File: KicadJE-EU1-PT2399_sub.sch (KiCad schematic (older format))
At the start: 57 parts, among them J201 In, J202 Out, P201 HEADER_2x5_Doepfer, Q201 BC337, Q202 PZT2222A, Q203 PZT2222A, U201 TL072, U202 PT2399

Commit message: Footprints
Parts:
- RV201: footprint Potentiometer_THT:Potentiometer_Alps_RK09K_Single_Vertical -> Potentiometer_THT:Potentiometer_China_RK09_Single_Vertical_AJ
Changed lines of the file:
@@
 	2550 1250 2550 1350
 $Comp
-L Eurorack:HEADER_2x5_Doepfer P201
+L Eurorack:HEADER_2x5_Doepfer P?
 U 1 1 5D631512
 P 2800 1350
-AR Path="/5D631512" Ref="P201"  Part="1"
+AR Path="/5D631512" Ref="P?"  Part="1"
 AR Path="/5D60ED9A/5D631512" Ref="P201"  Part="1"
 F 0 "P201" H 2800 852 40  0000 C CNN
@@
 	4050 1800 3725 1800
 $Comp
-L power:+5VA #PWR0201
+L power:+5VA #PWR0121
 U 1 1 5D64AB64
 P 4575 1150
-F 0 "#PWR0201" H 4575 1000 50  0001 C CNN
+F 0 "#PWR0121" H 4575 1000 50  0001 C CNN
 F 1 "+5VA" H 4590 1323 50  0000 C CNN
 F 2 "" H 4575 1150 50  0001 C CNN
@@
 $EndComp
 $Comp
-L power:+5VA #PWR0209
+L power:+5VA #PWR0122
 U 1 1 5D64D016
 P 3725 3550
-F 0 "#PWR0209" H 3725 3400 50  0001 C CNN
+F 0 "#PWR0122" H 3725 3400 50  0001 C CNN
 F 1 "+5VA" H 3740 3723 50  0000 C CNN
 F 2 "" H 3725 3550 50  0001 C CNN
@@
 Connection ~ 4425 1800
 $Comp
-L power:GNDA #PWR0206
+L power:GNDA #PWR0123
 U 1 1 5D64E4DB
 P 4425 2100
-F 0 "#PWR0206" H 4425 1850 50  0001 C CNN
+F 0 "#PWR0123" H 4425 1850 50  0001 C CNN
 F 1 "GNDA" H 4430 1927 50  0000 C CNN
 F 2 "" H 4425 2100 50  0001 C CNN
@@
 Connection ~ 4425 2100
 $Comp
-L power:GNDA #PWR0210
+L power:GNDA #PWR0124
 U 1 1 5D64E67F
 P 3425 3850
-F 0 "#PWR0210" H 3425 3600 50  0001 C CNN
+F 0 "#PWR0124" H 3425 3600 50  0001 C CNN
 F 1 "GNDA" H 3430 3677 50  0000 C CNN
 F 2 "" H 3425 3850 50  0001 C CNN
@@
 	3725 4450 3550 4450
 $Comp
-L power:GNDA #PWR0218
+L power:GNDA #PWR0125
 U 1 1 5D653327
 P 3700 4875
-F 0 "#PWR0218" H 3700 4625 50  0001 C CNN
+F 0 "#PWR0125" H 3700 4625 50  0001 C CNN
 F 1 "GNDA" H 3705 4702 50  0000 C CNN
 F 2 "" H 3700 4875 50  0001 C CNN
@@
 $EndComp
 $Comp
-L power:GNDA #PWR0217
+L power:GNDA #PWR0126
 U 1 1 5D653368
 P 3550 4750
-F 0 "#PWR0217" H 3550 4500 50  0001 C CNN
+F 0 "#PWR0126" H 3550 4500 50  0001 C CNN
 F 1 "GNDA" H 3555 4577 50  0000 C CNN
 F 2 "" H 3550 4750 50  0001 C CNN
@@
 Connection ~ 5675 4250
 $Comp
-L power:GNDA #PWR0215
+L power:GNDA #PWR0127
 U 1 1 5D6610CC
 P 5675 4450
-F 0 "#PWR0215" H 5675 4200 50  0001 C CNN
+F 0 "#PWR0127" H 5675 4200 50  0001 C CNN
 F 1 "GNDA" H 5680 4277 50  0000 C CNN
 F 2 "" H 5675 4450 50  0001 C CNN
@@
 $EndComp
 $Comp
-L power:GNDA #PWR0212
+L power:GNDA #PWR0128
 U 1 1 5D667A82
 P 5150 3975
-F 0 "#PWR0212" H 5150 3725 50  0001 C CNN
+F 0 "#PWR0128" H 5150 3725 50  0001 C CNN
 F 1 "GNDA" H 5155 3802 50  0000 C CNN
 F 2 "" H 5150 3975 50  0001 C CNN
@@
 F 0 "RV201" H 6075 3775 50  0000 R CNN
 F 1 "50k" H 6075 3850 50  0000 R CNN
-F 2 "Potentiometer_THT:Potentiometer_Alps_RK09K_Single_Vertical" H 5850 3925 50  0001 C CNN
+F 2 "Potentiometer_THT:Potentiometer_China_RK09_Single_Vertical_AJ" H 5850 3925 50  0001 C CNN
 F 3 "~" H 5850 3925 50  0001 C CNN
 	1    5850 3925
@@
 	5675 3775 5850 3775
 $Comp
-L power:GNDA #PWR0213
+L power:GNDA #PWR0129
 U 1 1 5D66F427
 P 5850 4075
-F 0 "#PWR0213" H 5850 3825 50  0001 C CNN
+F 0 "#PWR0129" H 5850 3825 50  0001 C CNN
 F 1 "GNDA" H 5950 3950 50  0000 C CNN
 F 2 "" H 5850 4075 50  0001 C CNN
@@
 $EndComp
 $Comp
-L power:GNDA #PWR0207
+L power:GNDA #PWR0130
 U 1 1 5D6945A7
 P 5025 3100
-F 0 "#PWR0207" H 5025 2850 50  0001 C CNN
+F 0 "#PWR0130" H 5025 2850 50  0001 C CNN
 F 1 "GNDA" H 5030 2927 50  0000 C CNN
 F 2 "" H 5025 3100 50  0001 C CNN
@@
 $EndComp
 $Comp
-L power:GNDA #PWR0208
+L power:GNDA #PWR0131
 U 1 1 5D694740
 P 6250 3375
-F 0 "#PWR0208" H 6250 3125 50  0001 C CNN
+F 0 "#PWR0131" H 6250 3125 50  0001 C CNN
 F 1 "GNDA" H 6255 3202 50  0000 C CNN
 F 2 "" H 6250 3375 50  0001 C CNN
@@
 	2650 4300 2650 4375
 $Comp
-L power:+5VA #PWR0214
+L power:+5VA #PWR0132
 U 1 1 5D6D7FCA
 P 2525 4375
-F 0 "#PWR0214" H 2525 4225 50  0001 C CNN
+F 0 "#PWR0132" H 2525 4225 50  0001 C CNN
 F 1 "+5VA" H 2540 4548 50  0000 C CNN
 F 2 "" H 2525 4375 50  0001 C CNN
@@
 	2825 5575 3050 5575
 $Comp
-L power:GNDA #PWR0220
+L power:GNDA #PWR0133
 U 1 1 5C5F26D3
 P 3050 5575
-F 0 "#PWR0220" H 3050 5325 50  0001 C CNN
+F 0 "#PWR0133" H 3050 5325 50  0001 C CNN
 F 1 "GNDA" H 3055 5402 50  0000 C CNN
 F 2 "" H 3050 5575 50  0001 C CNN

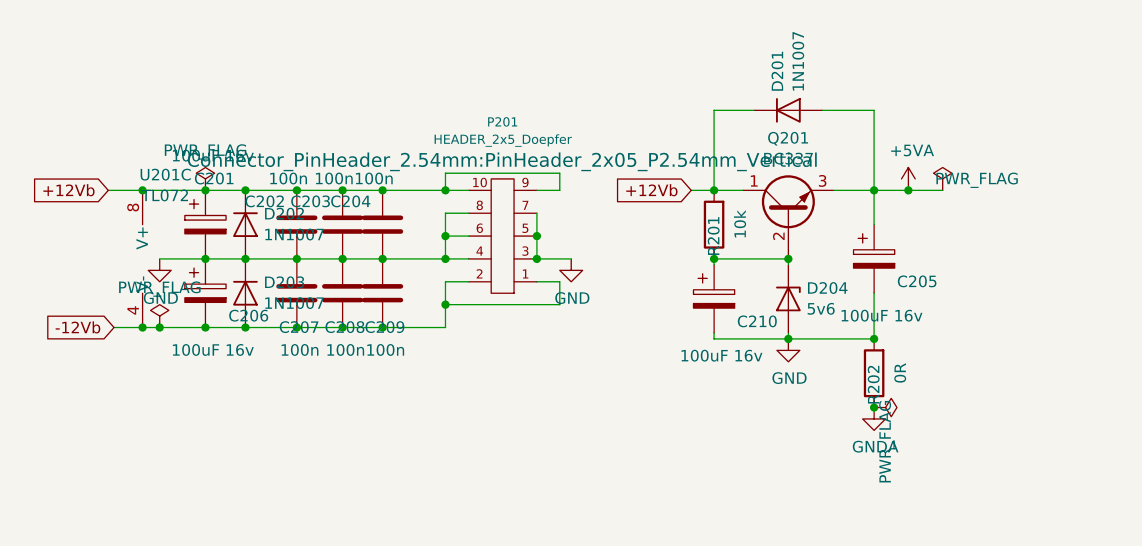
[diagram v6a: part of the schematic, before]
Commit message: Remove extra components from PT2399 and add EU3 diagram
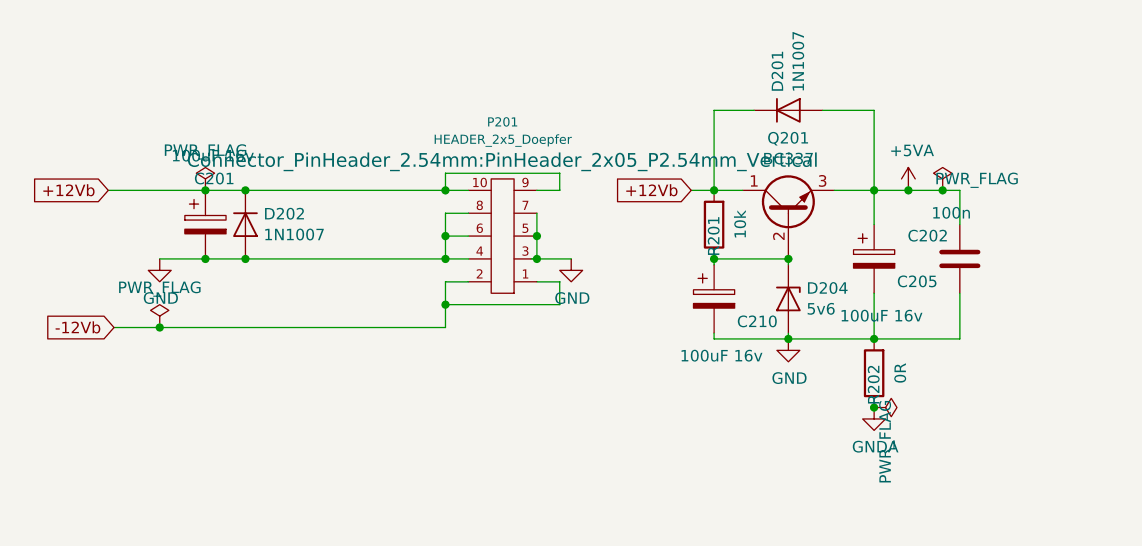
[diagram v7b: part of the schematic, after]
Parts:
- removed C203, C204, C207, C208, C209: 100n, Capacitor_SMD:C_0805_2012Metric_Pad1.15x1.40mm_HandSolder, symbol Device:C
- removed C206: 100uF 16v, Capacitor_THT:CP_Radial_D5.0mm_P2.50mm, symbol Device:CP
- removed D203: 1N1007, Diode_SMD:D_SOD-123, symbol Device:D
- removed U201: TL072, AJ-Dropbox-Kicad:AJ_SO-8_5.3x6.2mm_P1.27mm, symbol Amplifier_Operational:TL072
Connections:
- net +12Vb: no longer C202.2
- net +5VA: now also C202.2
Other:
- moved on the sheet: C202
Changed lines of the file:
@@
 $Descr A4 11693 8268
 encoding utf-8
-Sheet 2 2
+Sheet 2 3
 Title ""
 Date ""
@@
 $EndComp
 $Comp
-L Device:CP C?
-U 1 1 5D62F372
-P 1500 1600
-AR Path="/5D62F372" Ref="C?"  Part="1"
-AR Path="/5D60ED9A/5D62F372" Ref="C206"  Part="1"
-F 0 "C206" H 1600 1500 50  0000 L CNN
-F 1 "100uF 16v" H 1350 1350 50  0000 L CNN
-F 2 "Capacitor_THT:CP_Radial_D5.0mm_P2.50mm" H 1538 1450 50  0001 C CNN
-F 3 "~" H 1500 1600 50  0001 C CNN
-	1    1500 1600
-	1    0    0    -1
-$EndComp
-$Comp
 L power:GND #PWR?
 U 1 1 5D62F379
@@
 L Device:C C?
 U 1 1 5D62F383
-P 1900 1300
+P 4800 1450
 AR Path="/5D62F383" Ref="C?"  Part="1"
 AR Path="/5D60ED9A/5D62F383" Ref="C202"  Part="1"
-F 0 "C202" H 1950 1200 50  0000 L CNN
-F 1 "100n" H 1850 1100 50  0000 L CNN
-F 2 "Capacitor_SMD:C_0805_2012Metric_Pad1.15x1.40mm_HandSolder" H 1938 1150 50  0001 C CNN
-F 3 "~" H 1900 1300 50  0001 C CNN
-	1    1900 1300
+F 0 "C202" H 4850 1350 50  0000 L CNN
+F 1 "100n" H 4750 1250 50  0000 L CNN
+F 2 "Capacitor_SMD:C_0805_2012Metric_Pad1.15x1.40mm_HandSolder" H 4838 1300 50  0001 C CNN
+F 3 "~" H 4800 1450 50  0001 C CNN
+	1    4800 1450
 	-1   0    0    1
 $EndComp
-$Comp
-L Device:C C?
-U 1 1 5D62F38A
-P 1900 1600
-AR Path="/5D62F38A" Ref="C?"  Part="1"
-AR Path="/5D60ED9A/5D62F38A" Ref="C207"  Part="1"
-F 0 "C207" H 1800 1750 50  0000 L CNN
-F 1 "100n" H 1800 1850 50  0000 L CNN
-F 2 "Capacitor_SMD:C_0805_2012Metric_Pad1.15x1.40mm_HandSolder" H 1938 1450 50  0001 C CNN
-F 3 "~" H 1900 1600 50  0001 C CNN
-	1    1900 1600
-	-1   0    0    1
-$EndComp
 Wire Wire Line
 	1500 1450 1675 1450
-Connection ~ 1900 1450
 Wire Wire Line
 	1500 1150 1675 1150
 Connection ~ 1500 1150
 Wire Wire Line
-	1500 1750 1675 1750
-Connection ~ 1500 1750
-Connection ~ 1900 1150
-Connection ~ 1900 1750
-Wire Wire Line
 	3050 1650 3050 1550
-Wire Wire Line
-	1900 1150 2100 1150
-Wire Wire Line
-	1900 1450 2100 1450
 Wire Wire Line
 	2550 1550 2550 1650
@@
 	2550 1750 2550 1650
 Connection ~ 2550 1650
-Wire Wire Line
-	1900 1750 2100 1750
 $Comp
 L power:PWR_FLAG #FLG?
@@
 $EndComp
 Connection ~ 1300 1750
-Wire Wire Line
-	1300 1750 1500 1750
 Text GLabel 1100 1750 0    50   Input ~ 0
 -12Vb
 Text GLabel 1075 1150 0    50   Input ~ 0
 +12Vb
-$Comp
-L Device:C C?
-U 1 1 5D62F3E0
-P 2100 1600
-AR Path="/5D62F3E0" Ref="C?"  Part="1"
-AR Path="/5D60ED9A/5D62F3E0" Ref="C208"  Part="1"
-F 0 "C208" H 2000 1750 50  0000 L CNN
-F 1 "100n" H 2000 1850 50  0000 L CNN
-F 2 "Capacitor_SMD:C_0805_2012Metric_Pad1.15x1.40mm_HandSolder" H 2138 1450 50  0001 C CNN
-F 3 "~" H 2100 1600 50  0001 C CNN
-	1    2100 1600
-	-1   0    0    1
-$EndComp
-$Comp
-L Device:C C?
-U 1 1 5D62F3E7
-P 2100 1300
-AR Path="/5D62F3E7" Ref="C?"  Part="1"
-AR Path="/5D60ED9A/5D62F3E7" Ref="C203"  Part="1"
-F 0 "C203" H 2150 1200 50  0000 L CNN
-F 1 "100n" H 2050 1100 50  0000 L CNN
-F 2 "Capacitor_SMD:C_0805_2012Metric_Pad1.15x1.40mm_HandSolder" H 2138 1150 50  0001 C CNN
-F 3 "~" H 2100 1300 50  0001 C CNN
-	1    2100 1300
-	-1   0    0    1
-$EndComp
 $Comp
 L Device:D D?
@@
 $EndComp
 Connection ~ 1675 1150
-Wire Wire Line
-	1675 1150 1900 1150
 Connection ~ 1675 1450
-Wire Wire Line
-	1675 1450 1900 1450
-$Comp
-L Device:D D?
-U 1 1 5D62F3F9
-P 1675 1600
-AR Path="/5D62F3F9" Ref="D?"  Part="1"
-AR Path="/5D60ED9A/5D62F3F9" Ref="D203"  Part="1"
-F 0 "D203" V 1629 1679 50  0000 L CNN
-F 1 "1N1007" V 1720 1679 50  0000 L CNN
-F 2 "Diode_SMD:D_SOD-123" H 1675 1600 50  0001 C CNN
-F 3 "~" H 1675 1600 50  0001 C CNN
-	1    1675 1600
-	0    1    1    0
-$EndComp
-Connection ~ 1675 1750
-Wire Wire Line
-	1675 1750 1900 1750
-$Comp
-L Amplifier_Operational:TL072 U?
-U 3 1 5D62F402
-P 1325 1450
-AR Path="/5D62F402" Ref="U?"  Part="3"
-AR Path="/5D60ED9A/5D62F402" Ref="U201"  Part="3"
-F 0 "U201" H 1325 1817 50  0000 C CNN
-F 1 "TL072" H 1325 1726 50  0000 C CNN
-F 2 "AJ-Dropbox-Kicad:AJ_SO-8_5.3x6.2mm_P1.27mm" H 1325 1450 50  0001 C CNN
-F 3 "http://www.ti.com/lit/ds/symlink/tl071.pdf" H 1325 1450 50  0001 C CNN
-	3    1325 1450
-	1    0    0    -1
-$EndComp
-Connection ~ 1225 1750
-Wire Wire Line
-	1225 1750 1300 1750
-Connection ~ 1225 1150
-Wire Wire Line
-	1225 1150 1500 1150
-Connection ~ 2100 1750
-Connection ~ 2100 1450
-Connection ~ 2100 1150
-$Comp
-L Device:C C?
-U 1 1 5D62F410
-P 2275 1300
-AR Path="/5D62F410" Ref="C?"  Part="1"
-AR Path="/5D60ED9A/5D62F410" Ref="C204"  Part="1"
-F 0 "C204" H 2325 1200 50  0000 L CNN
-F 1 "100n" H 2225 1100 50  0000 L CNN
-F 2 "Capacitor_SMD:C_0805_2012Metric_Pad1.15x1.40mm_HandSolder" H 2313 1150 50  0001 C CNN
-F 3 "~" H 2275 1300 50  0001 C CNN
-	1    2275 1300
-	-1   0    0    1
-$EndComp
-Connection ~ 2275 1450
-Connection ~ 2275 1150
-$Comp
-L Device:C C?
-U 1 1 5D62F41B
-P 2275 1600
-AR Path="/5D62F41B" Ref="C?"  Part="1"
-AR Path="/5D60ED9A/5D62F41B" Ref="C209"  Part="1"
-F 0 "C209" H 2175 1750 50  0000 L CNN
-F 1 "100n" H 2175 1850 50  0000 L CNN
-F 2 "Capacitor_SMD:C_0805_2012Metric_Pad1.15x1.40mm_HandSolder" H 2313 1450 50  0001 C CNN
-F 3 "~" H 2275 1600 50  0001 C CNN
-	1    2275 1600
-	-1   0    0    1
-$EndComp
-Connection ~ 2275 1750
-Wire Wire Line
-	2275 1750 2550 1750
-Wire Wire Line
-	2100 1150 2275 1150
-Wire Wire Line
-	2100 1450 2275 1450
-Wire Wire Line
-	2100 1750 2275 1750
 Wire Wire Line
 	2550 1250 2550 1350
@@
 Connection ~ 2950 1450
 Wire Wire Line
-	2275 1150 2550 1150
-Wire Wire Line
 	2950 1150 3050 1150
 Wire Wire Line
@@
 Wire Wire Line
 	3725 1800 3725 1775
-Wire Wire Line
-	1100 1750 1225 1750
-Wire Wire Line
-	1075 1150 1225 1150
 Wire Wire Line
 	3900 800  3725 800
@@
 	1    0    0    -1
 $EndComp
-Wire Wire Line
-	2275 1450 2550 1450
 $Comp
 L power:GND #PWR?
@@
 Text GLabel 6525 1700 0    50   Input ~ 0
 Out
+Wire Wire Line
+	1100 1750 1300 1750
+Wire Wire Line
+	1075 1150 1500 1150
+Wire Wire Line
+	1300 1750 2550 1750
+Wire Wire Line
+	4425 1800 4800 1800
+Wire Wire Line
+	4800 1800 4800 1600
+Wire Wire Line
+	1675 1150 2550 1150
+Wire Wire Line
+	1675 1450 2550 1450
+Wire Wire Line
+	4800 1300 4800 1150
+Wire Wire Line
+	4800 1150 4725 1150
+Connection ~ 4725 1150
 $EndSCHEMATC

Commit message: GNDS and GNDA
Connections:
- net labels removed: -12Vb
- wire segments 138 -> 137
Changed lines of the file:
@@
 L power:PWR_FLAG #FLG?
 U 1 1 5D62F3D0
-P 1300 1750
+P 1875 1450
 AR Path="/5D62F3D0" Ref="#FLG?"  Part="1"
 AR Path="/5D60ED9A/5D62F3D0" Ref="#FLG0203"  Part="1"
-F 0 "#FLG0203" H 1300 1825 50  0001 C CNN
-F 1 "PWR_FLAG" H 1300 1924 50  0000 C CNN
-F 2 "" H 1300 1750 50  0001 C CNN
-F 3 "~" H 1300 1750 50  0001 C CNN
-	1    1300 1750
-	1    0    0    -1
-$EndComp
-Connection ~ 1300 1750
-Text GLabel 1100 1750 0    50   Input ~ 0
--12Vb
+F 0 "#FLG0203" H 1875 1525 50  0001 C CNN
+F 1 "PWR_FLAG" H 1875 1624 50  0000 C CNN
+F 2 "" H 1875 1450 50  0001 C CNN
+F 3 "~" H 1875 1450 50  0001 C CNN
+	1    1875 1450
+	1    0    0    -1
+$EndComp
 Text GLabel 1075 1150 0    50   Input ~ 0
 +12Vb
@@
 AR Path="/5D60ED9A/5D64AC58" Ref="#PWR0203"  Part="1"
 F 0 "#PWR0203" H 3100 1200 50  0001 C CNN
-F 1 "GND" H 3105 1277 50  0000 C CNN
+F 1 "GND" H 3200 1525 50  0000 C CNN
 F 2 "" H 3100 1450 50  0001 C CNN
 F 3 "" H 3100 1450 50  0001 C CNN
@@
 	2150 5650 2200 5650
 $Comp
-L power:GND #PWR?
+L power:GNDA #PWR?
 U 1 1 5D650219
 P 2450 5250
@@
 AR Path="/5D60ED9A/5D650219" Ref="#PWR0219"  Part="1"
 F 0 "#PWR0219" H 2450 5000 50  0001 C CNN
-F 1 "GND" H 2455 5077 50  0000 C CNN
+F 1 "GNDA" H 2455 5077 50  0000 C CNN
 F 2 "" H 2450 5250 50  0001 C CNN
 F 3 "" H 2450 5250 50  0001 C CNN
@@
 Voltage divider for \nVbe between 0 \nand 0,65v on the input
 $Comp
-L power:GND #PWR?
+L power:GNDA #PWR?
 U 1 1 5C60BCB0
 P 3000 4650
@@
 AR Path="/5D60ED9A/5C60BCB0" Ref="#PWR0216"  Part="1"
 F 0 "#PWR0216" H 3000 4400 50  0001 C CNN
-F 1 "GND" H 3005 4477 50  0000 C CNN
+F 1 "GNDA" H 3005 4477 50  0000 C CNN
 F 2 "" H 3000 4650 50  0001 C CNN
 F 3 "" H 3000 4650 50  0001 C CNN
@@
 Out
 Wire Wire Line
-	1100 1750 1300 1750
-Wire Wire Line
 	1075 1150 1500 1150
 Wire Wire Line
-	1300 1750 2550 1750
-Wire Wire Line
 	4425 1800 4800 1800
 Wire Wire Line
@@
 	1675 1150 2550 1150
 Wire Wire Line
-	1675 1450 2550 1450
+	1675 1450 1875 1450
 Wire Wire Line
 	4800 1300 4800 1150
@@
 	4800 1150 4725 1150
 Connection ~ 4725 1150
+Connection ~ 1875 1450
+Wire Wire Line
+	1875 1450 2550 1450
 $EndSCHEMATC
